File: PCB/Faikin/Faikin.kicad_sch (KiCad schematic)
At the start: 31 parts, among them J1 1x5, J2 TC2030-USB-NL, J3 Reset, Q1 BSS138PS, U3 MD8942, U4 ESP32-S3-MINI-1

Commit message: New PCB
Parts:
- removed C10: 100nF, RevK:C_0603_, symbol RevK:Hidden
- removed C8: 10uF 35V, RevK:C_0603_, symbol RevK:Hidden
- removed C9: 10uF 6.3V, RevK:C_0603_, symbol RevK:Hidden
- removed L2: 10uH, RevK:L_4x4_, symbol RevK:Hidden
- removed R10: 39k2, RevK:R_0402_, symbol RevK:Hidden
- removed R11: 1M, RevK:R_0402_, symbol RevK:Hidden
- removed R9: 124k, RevK:R_0402_, symbol RevK:Hidden
- removed U3: MD8942, RevK:SOT-23-6-MD8942, symbol RevK:MD89420-RegBlock
- added C1, C18, C4, C7: 100nF, RevK:C_0201, symbol Device:C
- added C15: 47uF 6V, RevK:C_0805, symbol Device:C
- added C16, C3: 100nF 25V, RevK:C_0402, symbol Device:C
- added C17: 22uF 25V, RevK:C_0805, symbol Device:C
- added C19: 18pF, RevK:C_0201, symbol Device:C
- added L1: 4.7uH, RevK:L_5x5, symbol Device:L
- added R5: 100k, RevK:R_0201, symbol Device:R
- added R6: 150k 1%, RevK:R_0201, symbol Device:R
- added R8: 33k 1%, RevK:R_0201, symbol Device:R
- added TP2, TP3, TP4, TP5, TP6: TestPoint, RevK:PAD-2mm, symbol Connector:TestPoint
- added U1: TPS562246, RevK:SOT-563, symbol RevK:TPS562246
- C2: footprint RevK:C_0402 -> RevK:C_0201; MPN (none) -> C76934
- C5: value 22uF -> 100nF; footprint RevK:C_0603 -> RevK:C_0201; MPN (none) -> C76934
- C6: footprint RevK:C_0402 -> RevK:C_0201
- R1, R2, R3: footprint RevK:R_0402 -> RevK:R_0201; MPN C25744 -> C106225
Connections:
- net +3.3V: now also C2.2, C5.2, C1.2, C15.1, C19.2, C4.2, C7.2, L1.2, R6.1, TP5.1; no longer C2.1, C5.1, U4.19 (GPIO15)
- net D+: now also TP3.1
- net D-: now also TP2.1
- net DC: now also C16.1, C17.1, C3.1, R5.1, U1.1 (VIN)
- net GND: now also C2.1, C5.1, U4.19 (GPIO15), C1.1, C15.2, C16.2, C17.2, C3.2, C4.1, C7.1, R8.2, TP4.1, U1.3 (GND); no longer C2.2, C5.2
- net RST: now reaches C6.1, R3.2, U4.45 (EN)
- net RST: now also TP6.1
- new net BST: C18.1, U1.4 (VBST)
- new net EN: R5.2, U1.5 (EN)
- new net FB: C19.1, R6.2, R8.1, U1.6 (VFB)
- new net SW: C18.2, L1.1, U1.2 (SW)
- no-connect marks 26 -> 25
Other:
- note added: "Regulator block - IC rated 3.3V 2A, but thermal considerations are based on typical usage."
- moved on the sheet: D1, TP1

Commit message: Library update
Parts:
- added TP7: TestPoint, RevK:PAD-2mm, symbol Connector:TestPoint
- TP2, TP3, TP4, TP5, TP6: now left out of the parts list
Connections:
- net DC: now also TP7.1
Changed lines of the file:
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@@
 		)
 	)
+	(global_label "DC"
+		(shape output)
+		(at 254.635 151.13 0)
+		(fields_autoplaced yes)
+		(effects
+			(font
+				(size 1.27 1.27)
+			)
+			(justify left)
+		)
+		(property "Intersheetrefs" "${INTERSHEET_REFS}"
+			(at 259.506 151.13 0)
+			(effects
+				(font
+					(size 1.27 1.27)
+				)
+				(justify left)
+				(hide yes)
+			)
+		)
+	)
 	(global_label "D+"
 		(shape bidirectional)
@@
 		(unit 1)
 		(exclude_from_sim no)
-		(in_bom yes)
+		(in_bom no)
 		(on_board yes)
 		(dnp no)
@@
 		(unit 1)
 		(exclude_from_sim no)
-		(in_bom yes)
+		(in_bom no)
 		(on_board yes)
 		(dnp no)
@@
 		(unit 1)
 		(exclude_from_sim no)
-		(in_bom yes)
+		(in_bom no)
 		(on_board yes)
 		(dnp no)
@@
 		(unit 1)
 		(exclude_from_sim no)
-		(in_bom yes)
+		(in_bom no)
 		(on_board yes)
 		(dnp no)
@@
 		(unit 1)
 		(exclude_from_sim no)
-		(in_bom yes)
+		(in_bom no)
 		(on_board yes)
 		(dnp no)
@@
 					(unit 1)
 				)
+			)
+		)
+	)
+	(symbol
+		(lib_id "Connector:TestPoint")
+		(at 254.635 151.13 90)
+		(unit 1)
+		(exclude_from_sim no)
+		(in_bom no)
+		(on_board yes)
+		(dnp no)
+		(fields_autoplaced yes)
+		(property "Reference" "TP7"
+			(at 251.333 146.3505 90)
+			(effects
+				(font
+					(size 1.27 1.27)
+				)
+			)
+		)
+		(property "Value" "TestPoint"
+			(at 251.333 148.7748 90)
+			(effects
+				(font
+					(size 1.27 1.27)
+				)
+			)
+		)
+		(property "Footprint" "RevK:PAD-2mm"
+			(at 254.635 146.05 0)
+			(effects
+				(font
+					(size 1.27 1.27)
+				)
+				(hide yes)
+			)
+		)
+		(property "Datasheet" "~"
+			(at 254.635 146.05 0)
+			(effects
+				(font
+					(size 1.27 1.27)
+				)
+				(hide yes)
+			)
+		)
+		(property "Description" "test point"
+			(at 254.635 151.13 0)
+			(effects
+				(font
+					(size 1.27 1.27)
+				)
+				(hide yes)
+			)
+		)
+		(pin "1"
+		)
+		(instances
+			(project "Faikin"
+				(path "/46c350bb-7de4-4e81-aafd-4af55e37aab0"
+					(reference "TP7")
+					(unit 1)
+				)

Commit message: Library update
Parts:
- R5: value 100k -> 150k 1%; MPN C106224 -> C310173
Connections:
- net DC: now also R5.2; no longer R5.1
- net EN: now also R5.1; no longer R5.2
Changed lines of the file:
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@@
+	)
+	(symbol
+		(lib_id "Device:R")
+		(at 64.135 173.99 270)
+		(unit 1)
+		(exclude_from_sim no)
+		(in_bom yes)
+		(on_board yes)
+		(dnp no)
+		(property "Reference" "R5"
+			(at 62.865 173.99 90)
+			(effects
+				(font
+					(size 1.27 1.27)
+				)
+				(justify left)
+			)
+		)
+		(property "Value" "150k 1%"
+			(at 61.722 171.45 90)
+			(effects
+				(font
+					(size 1.27 1.27)
+				)
+				(justify left)
+			)
+		)
+		(property "Footprint" "RevK:R_0201"
+			(at 64.135 172.212 90)
+			(effects
+				(font
+					(size 1.27 1.27)
+				)
+				(hide yes)
+			)
+		)
+		(property "Datasheet" "~"
+			(at 64.135 173.99 0)
+			(effects
+				(font
+					(size 1.27 1.27)
+				)
+				(hide yes)
+			)
+		)
+		(property "Description" "Resistor"
+			(at 64.135 173.99 0)
+			(effects
+				(font
+					(size 1.27 1.27)
+				)
+				(hide yes)
+			)
+		)
+		(property "MPN" "C310173"
+			(at 64.135 173.99 0)
+			(effects
+				(font
+					(size 1.27 1.27)
+				)
+				(hide yes)
+			)
+		)
+		(pin "1"
+		)
+		(pin "2"
+		)
+		(instances
+			(project "Faikin"
+				(path "/46c350bb-7de4-4e81-aafd-4af55e37aab0"
+					(reference "R5")
+					(unit 1)
+				)
+			)
+		)
 	)
 	(symbol
@@
 					(unit 1)
 				)
-			)
-		)
-	)
-	(symbol
-		(lib_id "Device:R")
-		(at 64.135 173.99 90)
-		(unit 1)
-		(exclude_from_sim no)
-		(in_bom yes)
-		(on_board yes)
-		(dnp no)
-		(property "Reference" "R5"
-			(at 64.262 171.704 90)
-			(effects
-				(font
-					(size 1.27 1.27)
-				)
-			)
-		)
-		(property "Value" "100k"
-			(at 64.262 173.99 90)
-			(effects
-				(font
-					(size 1.27 1.27)
-				)
-			)
-		)
-		(property "Footprint" "RevK:R_0201"
-			(at 64.135 175.768 90)
-			(effects
-				(font
-					(size 1.27 1.27)
-				)
-				(hide yes)
-			)
-		)
-		(property "Datasheet" "~"
-			(at 64.135 173.99 0)
-			(effects
-				(font
-					(size 1.27 1.27)
-				)
-				(hide yes)
-			)
-		)
-		(property "Description" "Resistor"
-			(at 64.135 173.99 0)
-			(effects
-				(font
-					(size 1.27 1.27)
-				)
-				(hide yes)
-			)
-		)
-		(property "MPN" "C106224"
-			(at 64.135 173.99 90)
-			(effects
-				(font
-					(size 1.27 1.27)
-				)
-				(hide yes)
-			)
-		)
-		(pin "1"
-		)
-		(pin "2"
-		)
-		(instances
-			(project "Faikin"
-				(path "/46c350bb-7de4-4e81-aafd-4af55e37aab0"
-					(reference "R5")
-					(unit 1)
-				)

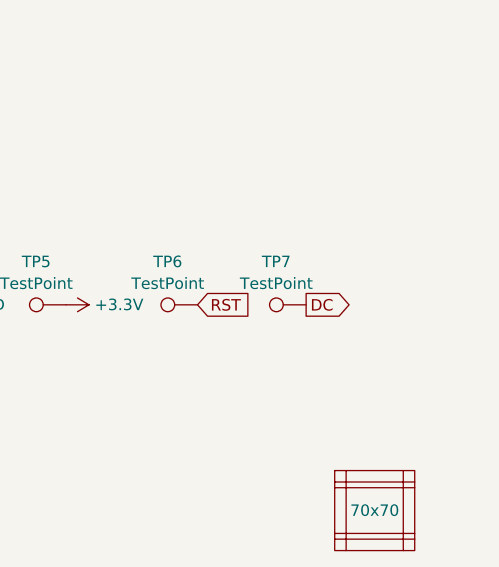
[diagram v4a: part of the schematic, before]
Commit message: Revised test points
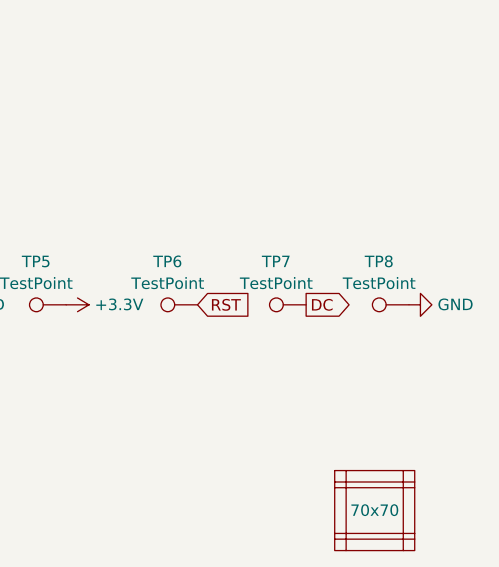
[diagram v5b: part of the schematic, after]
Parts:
- added TP8: TestPoint, RevK:PAD-2mm, symbol Connector:TestPoint
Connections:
- net GND: now also TP8.1
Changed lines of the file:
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@@
+	(symbol
+		(lib_id "power:GND")
+		(at 266.065 151.13 90)
+		(unit 1)
+		(exclude_from_sim no)
+		(in_bom yes)
+		(on_board yes)
+		(dnp no)
+		(fields_autoplaced yes)
+		(property "Reference" "#PWR05"
+			(at 272.415 151.13 0)
+			(effects
+				(font
+					(size 1.27 1.27)
+				)
+				(hide yes)
+			)
+		)
+		(property "Value" "GND"
+			(at 269.24 151.13 90)
+			(effects
+				(font
+					(size 1.27 1.27)
+				)
+				(justify right)
+			)
+		)
+		(property "Footprint" ""
+			(at 266.065 151.13 0)
+			(effects
+				(font
+					(size 1.27 1.27)
+				)
+				(hide yes)
+			)
+		)
+		(property "Datasheet" ""
+			(at 266.065 151.13 0)
+			(effects
+				(font
+					(size 1.27 1.27)
+				)
+				(hide yes)
+			)
+		)
+		(property "Description" "Power symbol creates a global label with name \"GND\" , ground"
+			(at 266.065 151.13 0)
+			(effects
+				(font
+					(size 1.27 1.27)
+				)
+				(hide yes)
+			)
+		)
+		(pin "1"
+		)
+		(instances
+			(project "Faikin"
+				(path "/46c350bb-7de4-4e81-aafd-4af55e37aab0"
+					(reference "#PWR05")
+					(unit 1)
+				)
+			)
+		)
+	)
+	(symbol
+		(lib_id "Connector:TestPoint")
+		(at 266.065 151.13 90)
+		(unit 1)
+		(exclude_from_sim no)
+		(in_bom no)
+		(on_board yes)
+		(dnp no)
+		(fields_autoplaced yes)
+		(property "Reference" "TP8"
+			(at 262.763 146.3505 90)
+			(effects
+				(font
+					(size 1.27 1.27)
+				)
+			)
+		)
+		(property "Value" "TestPoint"
+			(at 262.763 148.7748 90)
+			(effects
+				(font
+					(size 1.27 1.27)
+				)
+			)
+		)
+		(property "Footprint" "RevK:PAD-2mm"
+			(at 266.065 146.05 0)
+			(effects
+				(font
+					(size 1.27 1.27)
+				)
+				(hide yes)
+			)
+		)
+		(property "Datasheet" "~"
+			(at 266.065 146.05 0)
+			(effects
+				(font
+					(size 1.27 1.27)
+				)
+				(hide yes)
+			)
+		)
+		(property "Description" "test point"
+			(at 266.065 151.13 0)
+			(effects
+				(font
+					(size 1.27 1.27)
+				)
+				(hide yes)
+			)
+		)
+		(pin "1"
+		)
+		(instances
+			(project "Faikin"
+				(path "/46c350bb-7de4-4e81-aafd-4af55e37aab0"
+					(reference "TP8")
+					(unit 1)
+				)
+			)
+		)
+	)
 	(symbol
 		(lib_id "power:GND")

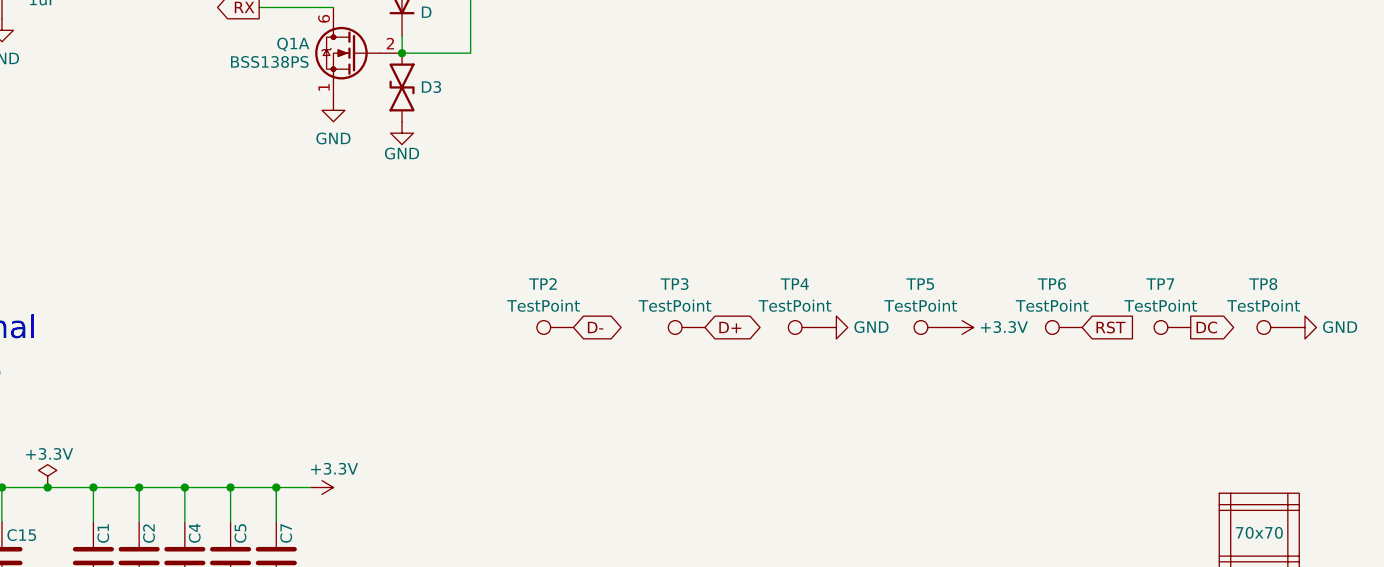
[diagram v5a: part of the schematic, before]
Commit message: Tweak layout, and more test points
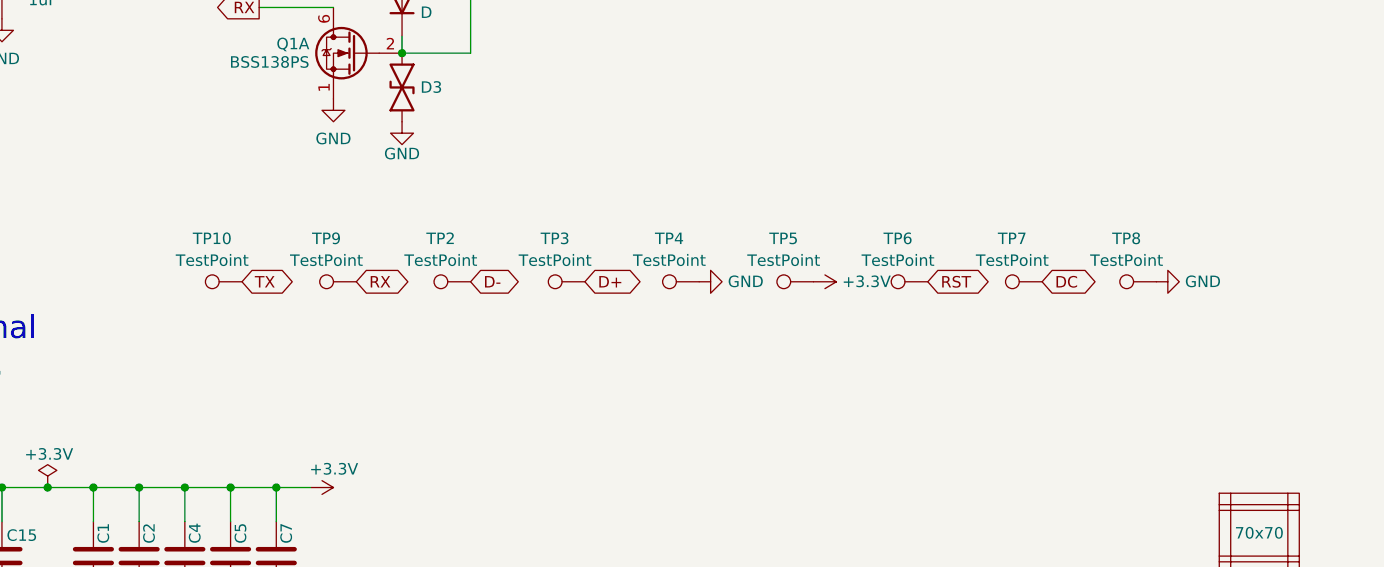
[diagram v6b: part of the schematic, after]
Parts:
- added TP10, TP9: TestPoint, RevK:PAD-2mm, symbol Connector:TestPoint
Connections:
- net RX: now also TP9.1
- net TX: now also TP10.1
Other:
- moved on the sheet: TP2, TP3, TP4, TP5, TP6, TP7, TP8

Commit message: Fiducials
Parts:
- added FID1, FID2, FID3: Fiducial, Fiducial:Fiducial_1mm_Mask2mm, symbol Mechanical:Fiducial
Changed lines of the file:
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@@
 	)
 	(symbol
+		(lib_id "Mechanical:Fiducial")
+		(at 90.805 118.745 0)
+		(unit 1)
+		(exclude_from_sim no)
+		(in_bom no)
+		(on_board yes)
+		(dnp no)
+		(fields_autoplaced yes)
+		(property "Reference" "FID1"
+			(at 92.964 117.5328 0)
+			(effects
+				(font
+					(size 1.27 1.27)
+				)
+				(justify left)
+			)
+		)
+		(property "Value" "Fiducial"
+			(at 92.964 119.9571 0)
+			(effects
+				(font
+					(size 1.27 1.27)
+				)
+				(justify left)
+			)
+		)
+		(property "Footprint" "Fiducial:Fiducial_1mm_Mask2mm"
+			(at 90.805 118.745 0)
+			(effects
+				(font
+					(size 1.27 1.27)
+				)
+				(hide yes)
+			)
+		)
+		(property "Datasheet" "~"
+			(at 90.805 118.745 0)
+			(effects
+				(font
+					(size 1.27 1.27)
+				)
+				(hide yes)
+			)
+		)
+		(property "Description" "Fiducial Marker"
+			(at 90.805 118.745 0)
+			(effects
+				(font
+					(size 1.27 1.27)
+				)
+				(hide yes)
+			)
+		)
+		(instances
+			(project ""
+				(path "/46c350bb-7de4-4e81-aafd-4af55e37aab0"
+					(reference "FID1")
+					(unit 1)
+				)
+			)
+		)
+	)
+	(symbol
+		(lib_id "Mechanical:Fiducial")
+		(at 90.805 123.825 0)
+		(unit 1)
+		(exclude_from_sim no)
+		(in_bom no)
+		(on_board yes)
+		(dnp no)
+		(fields_autoplaced yes)
+		(property "Reference" "FID2"
+			(at 92.964 122.6128 0)
+			(effects
+				(font
+					(size 1.27 1.27)
+				)
+				(justify left)
+			)
+		)
+		(property "Value" "Fiducial"
+			(at 92.964 125.0371 0)
+			(effects
+				(font
+					(size 1.27 1.27)
+				)
+				(justify left)
+			)
+		)
+		(property "Footprint" "Fiducial:Fiducial_1mm_Mask2mm"
+			(at 90.805 123.825 0)
+			(effects
+				(font
+					(size 1.27 1.27)
+				)
+				(hide yes)
+			)
+		)
+		(property "Datasheet" "~"
+			(at 90.805 123.825 0)
+			(effects
+				(font
+					(size 1.27 1.27)
+				)
+				(hide yes)
+			)
+		)
+		(property "Description" "Fiducial Marker"
+			(at 90.805 123.825 0)
+			(effects
+				(font
+					(size 1.27 1.27)
+				)
+				(hide yes)
+			)
+		)
+		(instances
+			(project "Faikin"
+				(path "/46c350bb-7de4-4e81-aafd-4af55e37aab0"
+					(reference "FID2")
+					(unit 1)
+				)
+			)
+		)
+	)
+	(symbol
 		(lib_id "RevK:TPS562246")
 		(at 80.01 171.45 0)
@@
 					(unit 1)
 				)
+			)
+		)
+	)
+	(symbol
+		(lib_id "Mechanical:Fiducial")
+		(at 90.805 128.905 0)
+		(unit 1)
+		(exclude_from_sim no)
+		(in_bom no)
+		(on_board yes)
+		(dnp no)
+		(fields_autoplaced yes)
+		(property "Reference" "FID3"
+			(at 92.964 127.6928 0)
+			(effects
+				(font
+					(size 1.27 1.27)
+				)
+				(justify left)
+			)
+		)
+		(property "Value" "Fiducial"
+			(at 92.964 130.1171 0)
+			(effects
+				(font
+					(size 1.27 1.27)
+				)
+				(justify left)
+			)
+		)
+		(property "Footprint" "Fiducial:Fiducial_1mm_Mask2mm"
+			(at 90.805 128.905 0)
+			(effects
+				(font
+					(size 1.27 1.27)
+				)
+				(hide yes)
+			)
+		)
+		(property "Datasheet" "~"
+			(at 90.805 128.905 0)
+			(effects
+				(font
+					(size 1.27 1.27)
+				)
+				(hide yes)
+			)
+		)
+		(property "Description" "Fiducial Marker"
+			(at 90.805 128.905 0)
+			(effects
+				(font
+					(size 1.27 1.27)
+				)
+				(hide yes)
+			)
+		)
+		(instances
+			(project "Faikin"
+				(path "/46c350bb-7de4-4e81-aafd-4af55e37aab0"
+					(reference "FID3")
+					(unit 1)
+				)
